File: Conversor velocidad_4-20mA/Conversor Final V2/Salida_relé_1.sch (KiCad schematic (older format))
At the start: 22 parts, among them Q2 BC848, U5 TL082

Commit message: Agregue footprints
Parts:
- C4, C5, C6: footprint (none) -> Capacitor_SMD:C_0603_1608Metric_Pad1.08x0.95mm_HandSolder
- D2, D4: footprint (none) -> Diode_SMD:D_0603_1608Metric_Pad1.05x0.95mm_HandSolder
- R10, R11, R12, R13, R14, R15, R16, R17, R18, R7, R8, R9, RV2: footprint (none) -> Resistor_SMD:R_0603_1608Metric_Pad0.98x0.95mm_HandSolder
- U5: footprint (none) -> Package_SO:HSOP-8-1EP_3.9x4.9mm_P1.27mm_EP2.41x3.1mm_ThermalVias
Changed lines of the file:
@@
 F 0 "R7" V 1043 4550 50  0000 C CNN
 F 1 "100K" V 1134 4550 50  0000 C CNN
-F 2 "" V 1180 4550 50  0001 C CNN
+F 2 "Resistor_SMD:R_0603_1608Metric_Pad0.98x0.95mm_HandSolder" V 1180 4550 50  0001 C CNN
 F 3 "~" H 1250 4550 50  0001 C CNN
 	1    1250 4550
@@
 F 0 "C4" H 1765 4796 50  0000 L CNN
 F 1 "1uF" H 1765 4705 50  0000 L CNN
-F 2 "" H 1688 4600 50  0001 C CNN
+F 2 "Capacitor_SMD:C_0603_1608Metric_Pad1.08x0.95mm_HandSolder" H 1688 4600 50  0001 C CNN
 F 3 "~" H 1650 4750 50  0001 C CNN
 	1    1650 4750
@@
 F 0 "R8" V 1793 4550 50  0000 C CNN
 F 1 "100K" V 1884 4550 50  0000 C CNN
-F 2 "" V 1930 4550 50  0001 C CNN
+F 2 "Resistor_SMD:R_0603_1608Metric_Pad0.98x0.95mm_HandSolder" V 1930 4550 50  0001 C CNN
 F 3 "~" H 2000 4550 50  0001 C CNN
 	1    2000 4550
@@
 F 0 "C5" H 2415 4796 50  0000 L CNN
 F 1 "1uF" H 2415 4705 50  0000 L CNN
-F 2 "" H 2338 4600 50  0001 C CNN
+F 2 "Capacitor_SMD:C_0603_1608Metric_Pad1.08x0.95mm_HandSolder" H 2338 4600 50  0001 C CNN
 F 3 "~" H 2300 4750 50  0001 C CNN
 	1    2300 4750
@@
 F 0 "R9" V 2643 4550 50  0000 C CNN
 F 1 "10K" V 2734 4550 50  0000 C CNN
-F 2 "" V 2780 4550 50  0001 C CNN
+F 2 "Resistor_SMD:R_0603_1608Metric_Pad0.98x0.95mm_HandSolder" V 2780 4550 50  0001 C CNN
 F 3 "~" H 2850 4550 50  0001 C CNN
 	1    2850 4550
@@
 F 0 "U5" H 5900 4717 50  0000 C CNN
 F 1 "TL082" H 5900 4626 50  0000 C CNN
-F 2 "" H 5900 4350 50  0001 C CNN
+F 2 "Package_SO:HSOP-8-1EP_3.9x4.9mm_P1.27mm_EP2.41x3.1mm_ThermalVias" H 5900 4350 50  0001 C CNN
 F 3 "http://www.ti.com/lit/ds/symlink/tl081.pdf" H 5900 4350 50  0001 C CNN
 	1    5900 4350
@@
 F 0 "U5" H 3700 4817 50  0000 C CNN
 F 1 "TL082" H 3700 4726 50  0000 C CNN
-F 2 "" H 3700 4450 50  0001 C CNN
+F 2 "Package_SO:HSOP-8-1EP_3.9x4.9mm_P1.27mm_EP2.41x3.1mm_ThermalVias" H 3700 4450 50  0001 C CNN
 F 3 "http://www.ti.com/lit/ds/symlink/tl081.pdf" H 3700 4450 50  0001 C CNN
 	2    3700 4450
@@
 F 0 "R10" V 3543 3850 50  0000 C CNN
 F 1 "10M" V 3634 3850 50  0000 C CNN
-F 2 "" V 3680 3850 50  0001 C CNN
+F 2 "Resistor_SMD:R_0603_1608Metric_Pad0.98x0.95mm_HandSolder" V 3680 3850 50  0001 C CNN
 F 3 "~" H 3750 3850 50  0001 C CNN
 	1    3750 3850
@@
 F 0 "RV2" H 3580 2554 50  0000 R CNN
 F 1 "10K" H 3580 2645 50  0000 R CNN
-F 2 "" H 3650 2600 50  0001 C CNN
+F 2 "Resistor_SMD:R_0603_1608Metric_Pad0.98x0.95mm_HandSolder" H 3650 2600 50  0001 C CNN
 F 3 "~" H 3650 2600 50  0001 C CNN
 	1    3650 2600
@@
 F 0 "R11" H 4220 3196 50  0000 L CNN
 F 1 "47K" H 4220 3105 50  0000 L CNN
-F 2 "" V 4080 3150 50  0001 C CNN
+F 2 "Resistor_SMD:R_0603_1608Metric_Pad0.98x0.95mm_HandSolder" V 4080 3150 50  0001 C CNN
 F 3 "~" H 4150 3150 50  0001 C CNN
 	1    4150 3150
@@
 F 0 "R12" H 4220 2096 50  0000 L CNN
 F 1 "68K" H 4220 2005 50  0000 L CNN
-F 2 "" V 4080 2050 50  0001 C CNN
+F 2 "Resistor_SMD:R_0603_1608Metric_Pad0.98x0.95mm_HandSolder" V 4080 2050 50  0001 C CNN
 F 3 "~" H 4150 2050 50  0001 C CNN
 	1    4150 2050
@@
 F 0 "R13" V 4543 4450 50  0000 C CNN
 F 1 "2.2M" V 4634 4450 50  0000 C CNN
-F 2 "" V 4680 4450 50  0001 C CNN
+F 2 "Resistor_SMD:R_0603_1608Metric_Pad0.98x0.95mm_HandSolder" V 4680 4450 50  0001 C CNN
 F 3 "~" H 4750 4450 50  0001 C CNN
 	1    4750 4450
@@
 F 0 "D2" H 4750 4267 50  0000 C CNN
 F 1 "FD300" H 4750 4176 50  0000 C CNN
-F 2 "" H 4750 4050 50  0001 C CNN
+F 2 "Diode_SMD:D_0603_1608Metric_Pad1.05x0.95mm_HandSolder" H 4750 4050 50  0001 C CNN
 F 3 "~" H 4750 4050 50  0001 C CNN
 	1    4750 4050
@@
 F 0 "C6" H 5065 4796 50  0000 L CNN
 F 1 "2.2uF" H 5065 4705 50  0000 L CNN
-F 2 "" H 4988 4600 50  0001 C CNN
+F 2 "Capacitor_SMD:C_0603_1608Metric_Pad1.08x0.95mm_HandSolder" H 4988 4600 50  0001 C CNN
 F 3 "~" H 4950 4750 50  0001 C CNN
 	1    4950 4750
@@
 F 0 "R14" V 5093 4450 50  0000 C CNN
 F 1 "10K" V 5184 4450 50  0000 C CNN
-F 2 "" V 5230 4450 50  0001 C CNN
+F 2 "Resistor_SMD:R_0603_1608Metric_Pad0.98x0.95mm_HandSolder" V 5230 4450 50  0001 C CNN
 F 3 "~" H 5300 4450 50  0001 C CNN
 	1    5300 4450
@@
 F 0 "R15" V 5693 3750 50  0000 C CNN
 F 1 "10M" V 5784 3750 50  0000 C CNN
-F 2 "" V 5830 3750 50  0001 C CNN
+F 2 "Resistor_SMD:R_0603_1608Metric_Pad0.98x0.95mm_HandSolder" V 5830 3750 50  0001 C CNN
 F 3 "~" H 5900 3750 50  0001 C CNN
 	1    5900 3750
@@
 F 0 "R16" H 6270 3046 50  0000 L CNN
 F 1 "R" H 6270 2955 50  0000 L CNN
-F 2 "" V 6130 3000 50  0001 C CNN
+F 2 "Resistor_SMD:R_0603_1608Metric_Pad0.98x0.95mm_HandSolder" V 6130 3000 50  0001 C CNN
 F 3 "~" H 6200 3000 50  0001 C CNN
 	1    6200 3000
@@
 F 0 "R17" H 6270 2096 50  0000 L CNN
 F 1 "R" H 6270 2005 50  0000 L CNN
-F 2 "" V 6130 2050 50  0001 C CNN
+F 2 "Resistor_SMD:R_0603_1608Metric_Pad0.98x0.95mm_HandSolder" V 6130 2050 50  0001 C CNN
 F 3 "~" H 6200 2050 50  0001 C CNN
 	1    6200 2050
@@
 F 0 "U5" H 4958 2296 50  0000 L CNN
 F 1 "TL082" H 4958 2205 50  0000 L CNN
-F 2 "" H 5000 2250 50  0001 C CNN
+F 2 "Package_SO:HSOP-8-1EP_3.9x4.9mm_P1.27mm_EP2.41x3.1mm_ThermalVias" H 5000 2250 50  0001 C CNN
 F 3 "http://www.ti.com/lit/ds/symlink/tl081.pdf" H 5000 2250 50  0001 C CNN
 	3    5000 2250
@@
 F 0 "R18" V 6957 4350 50  0000 C CNN
 F 1 "6.8K" V 6866 4350 50  0000 C CNN
-F 2 "" V 6680 4350 50  0001 C CNN
+F 2 "Resistor_SMD:R_0603_1608Metric_Pad0.98x0.95mm_HandSolder" V 6680 4350 50  0001 C CNN
 F 3 "~" H 6750 4350 50  0001 C CNN
 	1    6750 4350
@@
 F 0 "D4" V 7439 4682 50  0000 R CNN
 F 1 "LED" V 7348 4682 50  0000 R CNN
-F 2 "" H 7400 4800 50  0001 C CNN
+F 2 "Diode_SMD:D_0603_1608Metric_Pad1.05x0.95mm_HandSolder" H 7400 4800 50  0001 C CNN
 F 3 "~" H 7400 4800 50  0001 C CNN
 	1    7400 4800

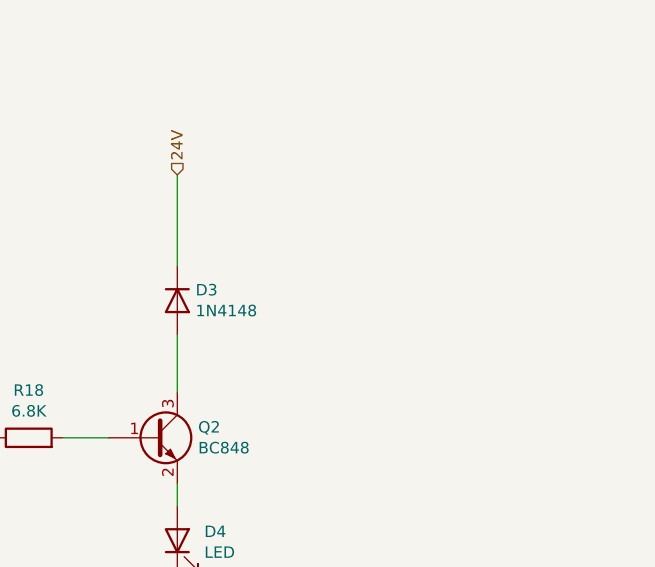
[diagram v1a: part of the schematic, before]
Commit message: Actualizacion Esquematico en bloques
Agregue un par de footprints y acomodé el relé en el bloque correspondiente. Hay que consultar sobre los footprint del 4040 y 4070
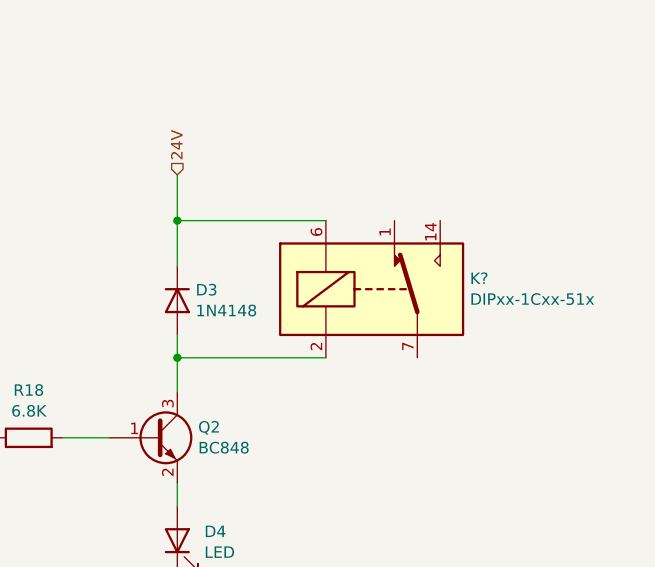
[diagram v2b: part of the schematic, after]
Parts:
- added K?: DIPxx-1Cxx-51x, Relay_THT:Relay_StandexMeder_DIP_LowProfile, symbol Relay:DIPxx-1Cxx-51x
- RV2: footprint Resistor_SMD:R_0603_1608Metric_Pad0.98x0.95mm_HandSolder -> (none)
- U5: footprint Package_SO:HSOP-8-1EP_3.9x4.9mm_P1.27mm_EP2.41x3.1mm_ThermalVias -> Package_SO:SOIC-8-1EP_3.9x4.9mm_P1.27mm_EP2.29x3mm
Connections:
- net 24V: now also K?.6
- net at D3.2 (A), Q2.3 (C): now also K?.2
- new net: K?.7, K?.8
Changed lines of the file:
@@
 F 0 "U5" H 5900 4717 50  0000 C CNN
 F 1 "TL082" H 5900 4626 50  0000 C CNN
-F 2 "Package_SO:HSOP-8-1EP_3.9x4.9mm_P1.27mm_EP2.41x3.1mm_ThermalVias" H 5900 4350 50  0001 C CNN
-F 3 "http://www.ti.com/lit/ds/symlink/tl081.pdf" H 5900 4350 50  0001 C CNN
+F 2 "Package_SO:SOIC-8-1EP_3.9x4.9mm_P1.27mm_EP2.29x3mm" H 5900 4350 50  0001 C CNN
+F 3 "https://www.digikey.com/es/products/detail/texas-instruments/TL082CDE4/13472954" H 5900 4350 50  0001 C CNN
 	1    5900 4350
 	1    0    0    -1
@@
 F 0 "U5" H 3700 4817 50  0000 C CNN
 F 1 "TL082" H 3700 4726 50  0000 C CNN
-F 2 "Package_SO:HSOP-8-1EP_3.9x4.9mm_P1.27mm_EP2.41x3.1mm_ThermalVias" H 3700 4450 50  0001 C CNN
-F 3 "http://www.ti.com/lit/ds/symlink/tl081.pdf" H 3700 4450 50  0001 C CNN
+F 2 "Package_SO:SOIC-8-1EP_3.9x4.9mm_P1.27mm_EP2.29x3mm" H 3700 4450 50  0001 C CNN
+F 3 "https://www.digikey.com/es/products/detail/texas-instruments/TL082CDE4/13472954" H 3700 4450 50  0001 C CNN
 	2    3700 4450
 	1    0    0    -1
@@
 F 0 "RV2" H 3580 2554 50  0000 R CNN
 F 1 "10K" H 3580 2645 50  0000 R CNN
-F 2 "Resistor_SMD:R_0603_1608Metric_Pad0.98x0.95mm_HandSolder" H 3650 2600 50  0001 C CNN
+F 2 "" H 3650 2600 50  0001 C CNN
 F 3 "~" H 3650 2600 50  0001 C CNN
 	1    3650 2600
@@
 F 0 "U5" H 4958 2296 50  0000 L CNN
 F 1 "TL082" H 4958 2205 50  0000 L CNN
-F 2 "Package_SO:HSOP-8-1EP_3.9x4.9mm_P1.27mm_EP2.41x3.1mm_ThermalVias" H 5000 2250 50  0001 C CNN
-F 3 "http://www.ti.com/lit/ds/symlink/tl081.pdf" H 5000 2250 50  0001 C CNN
+F 2 "Package_SO:SOIC-8-1EP_3.9x4.9mm_P1.27mm_EP2.29x3mm" H 5000 2250 50  0001 C CNN
+F 3 "https://www.digikey.com/es/products/detail/texas-instruments/TL082CDE4/13472954" H 5000 2250 50  0001 C CNN
 	3    5000 2250
 	1    0    0    -1
@@
 $EndComp
 Wire Wire Line
-	7400 4150 7400 3900
+	7400 4150 7400 4000
 Text HLabel 7400 3200 1    50   Input ~ 0
 24V
 Wire Wire Line
-	7400 3200 7400 3600
+	7400 3200 7400 3400
+$Comp
+L Relay:DIPxx-1Cxx-51x K?
+U 1 1 61350345
+P 8250 3700
+AR Path="/61350345" Ref="K?"  Part="1"
+AR Path="/61322896/61350345" Ref="K?"  Part="1"
+F 0 "K?" H 8680 3746 50  0000 L CNN
+F 1 "DIPxx-1Cxx-51x" H 8680 3655 50  0000 L CNN
+F 2 "Relay_THT:Relay_StandexMeder_DIP_LowProfile" H 8700 3650 50  0001 L CNN
+F 3 "https://standexelectronics.com/wp-content/uploads/datasheet_reed_relay_DIP.pdf" H 8250 3700 50  0001 C CNN
+	1    8250 3700
+	1    0    0    -1
+$EndComp
+Wire Wire Line
+	8050 3400 7400 3400
+Connection ~ 7400 3400
+Wire Wire Line
+	7400 3400 7400 3600
+Wire Wire Line
+	8050 4000 7400 4000
+Connection ~ 7400 4000
+Wire Wire Line
+	7400 4000 7400 3900
 $EndSCHEMATC
